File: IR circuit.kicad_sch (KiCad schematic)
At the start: 8 parts, among them J18 Conn_01x03_Pin, U3 LM2902

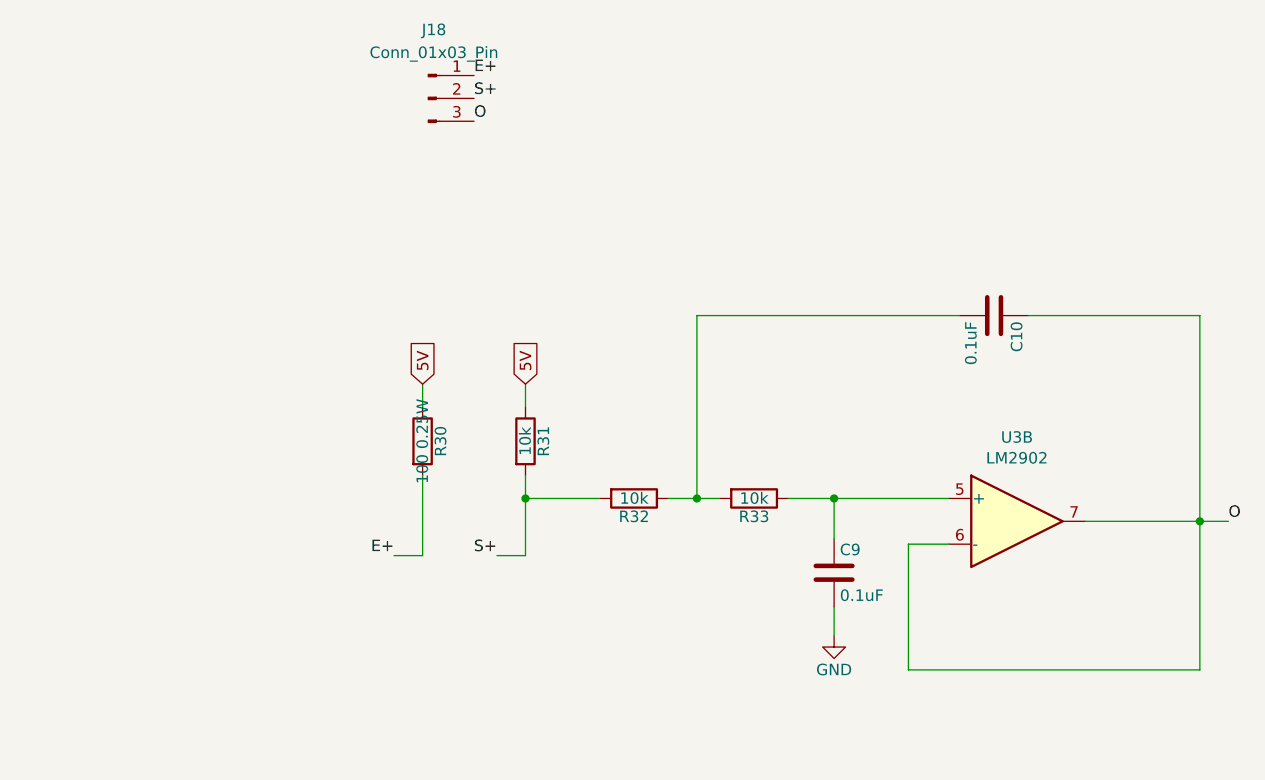
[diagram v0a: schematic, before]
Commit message: Add more ground pins. Fix labels.
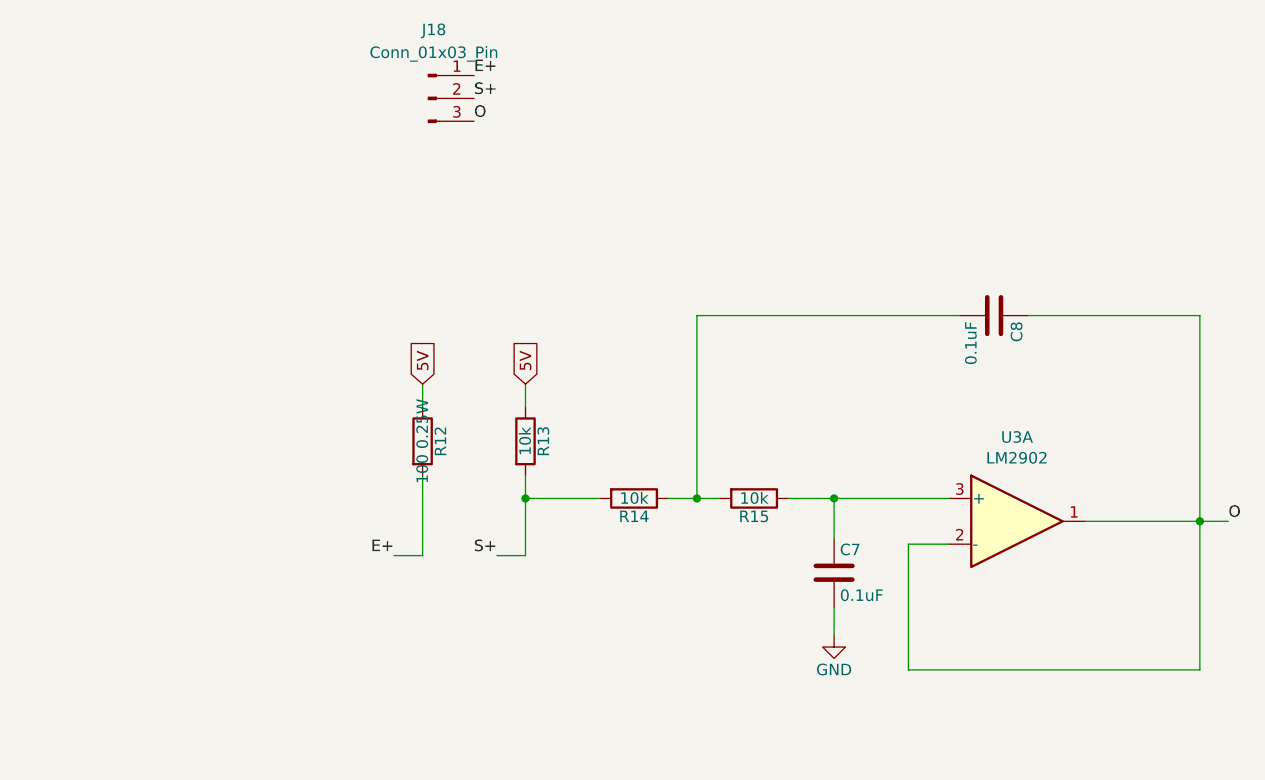
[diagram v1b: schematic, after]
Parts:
- C7: renamed from C9; footprint Capacitor_THT:C_Rect_L7.0mm_W3.5mm_P5.00mm -> Capacitor_THT:C_Rect_L4.0mm_W2.5mm_P2.50mm
- C8: renamed from C10; footprint Capacitor_THT:C_Rect_L7.0mm_W3.5mm_P5.00mm -> Capacitor_THT:C_Rect_L4.0mm_W2.5mm_P2.50mm
- renumbered R30 to R12, R31 to R13, R32 to R14, R33 to R15
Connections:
- net O: now also U3.1, U3.2 (-); no longer U3.6 (-), U3.7
- net at C7.1, R15.1: now also U3.3 (+); no longer U3.5 (+)

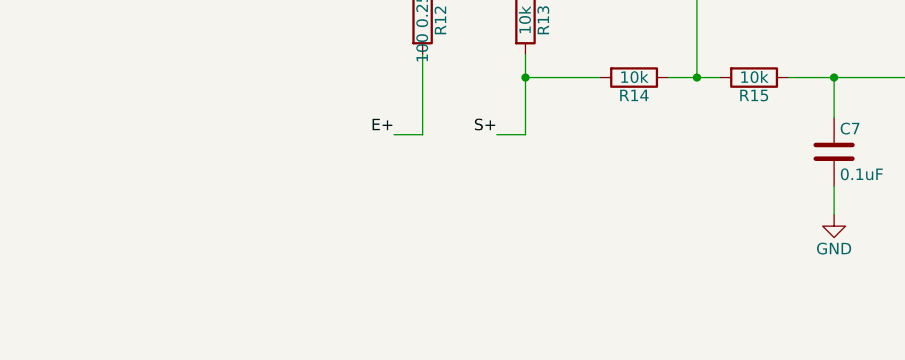
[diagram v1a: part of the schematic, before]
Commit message: Add documentation re IR circuit
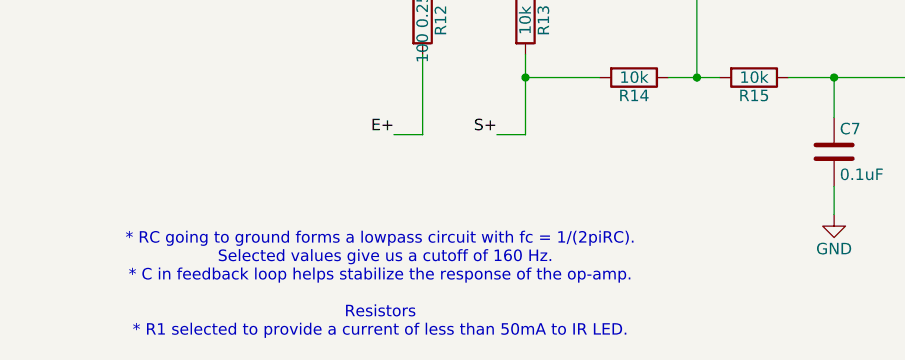
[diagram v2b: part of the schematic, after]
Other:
- note added: "* RC going to ground forms a lowpass circuit with fc = 1/(2piRC). Selected values give us a cutoff of 160 Hz. * C in feedback loop helps stabilize the response of the op-amp. Resistors * R1 selected to provide a current of less than 50mA to IR LED."
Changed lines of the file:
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@@
+		)
+	)
+	(text "* RC going to ground forms a lowpass circuit with fc = 1/(2piRC).\n  Selected values give us a cutoff of 160 Hz.\n* C in feedback loop helps stabilize the response of the op-amp.\n\nResistors\n* R1 selected to provide a current of less than 50mA to IR LED."
+		(exclude_from_sim no)
+		(at 111.506 112.014 0)
+		(effects
+			(font
+				(size 1.27 1.27)
+			)
 		)
 	)
